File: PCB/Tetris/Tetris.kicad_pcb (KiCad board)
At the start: 2 copper layers, 135 x 56 mm, 51 parts, among them J1 Power, J2 PWM, J3 Analog, J4 PWM, J5 Analog, J6 Communication, J7 Digital, M1 RGBMatrix, M2 RGBMatrix, SW1 SW_Push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

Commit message: MASSIVE PROGRESS
Redesign PCB to use ports
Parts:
- removed U2: 74HC595, Package_DIP:DIP-16_W7.62mm_Socket_LongPads
- added J8: Digital, Connector_PinHeader_2.54mm:PinHeader_2x08_P2.54mm_Vertical, B.Cu at (188.4, 125.4)
- G2: renamed from Mr. G
- J1: footprint Connector_PinHeader_2.54mm:PinHeader_1x08_P2.54mm_Vertical -> Connector_PinHeader_2.54mm:PinHeader_1x02_P2.54mm_Vertical
- J2: footprint Connector_PinHeader_2.54mm:PinHeader_1x10_P2.54mm_Vertical -> Connector_PinHeader_2.54mm:PinHeader_1x07_P2.54mm_Vertical
- J4: footprint Connector_PinHeader_2.54mm:PinHeader_1x08_P2.54mm_Vertical -> Connector_PinHeader_2.54mm:PinHeader_1x06_P2.54mm_Vertical
- J7: footprint Connector_PinHeader_2.54mm:PinHeader_2x18_P2.54mm_Vertical -> Connector_PinHeader_2.54mm:PinHeader_2x09_P2.54mm_Vertical
- R1, R10, R11, R12, R2, R24, R25, R26, R27, R3, R4, R5, R6, R7, R8, R9: footprint Resistor_THT:R_Axial_DIN0207_L6.3mm_D2.5mm_P10.16mm_Horizontal -> RGBMatrix:R_Axial_DIN0207_L6.3mm_D2.5mm_P12.40mm_Horizontal
- R17, R18: footprint Resistor_THT:R_Axial_DIN0207_L6.3mm_D2.5mm_P10.16mm_Horizontal -> Resistor_THT:R_Axial_DIN0207_L6.3mm_D2.5mm_P7.62mm_Horizontal
- moved BZ1 74.1 mm to (159.2, 72.5), turned to 180 degrees
- moved R24 70.1 mm to (161.9, 77.0), turned to 180 degrees
- moved BZ2 63.3 mm to (144.3, 72.5), turned to 180 degrees
- moved BZ4 57.6 mm to (111.8, 72.7), turned to 180 degrees
- moved R25 57.3 mm to (146.7, 77.0), turned to 180 degrees
- moved BZ3 57.2 mm to (129.1, 72.7), turned to 180 degrees
- moved R26 50.1 mm to (131.7, 77.0), turned to 180 degrees
- moved R27 49.6 mm to (114.3, 76.8), turned to 180 degrees
- moved R23 27.1 mm to (206.1, 112.7), turned to -90 degrees
- moved SW5 26.9 mm to (202.9, 87.8), turned to -90 degrees
- moved R20 26.7 mm to (216.9, 126.7), turned to 90 degrees
- moved R19 25.6 mm to (216.9, 113.7), turned to 90 degrees
- moved SW6 24.9 mm to (202.9, 98.8), turned to -90 degrees
- moved R17 23.2 mm to (216.8, 89.6), turned to 90 degrees
- moved J7 22.9 mm to (188.4, 102.5)
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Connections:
- BZ1 pad 1: /*13 -> /*6
- BZ2 pad 1: /*12 -> /*7
- BZ3 pad 1: /*11 -> /*8
- BZ4 pad 1: /*10 -> /*9
- J1 pad 1: unconnected-(J1-Pin_1-Pad1) -> +5V
- J1 pad 2: /IOREF -> GND
- J2 pad 1: /SCL/21 -> GND
- J2 pad 2: /SDA/20 -> /*13
- J2 pad 3: /AREF -> /*12
- J2 pad 4: GND -> /*11
- J2 pad 5: /*13 -> /*10
- J2 pad 6: /*12 -> /*9
- J2 pad 7: /*11 -> /*8
- J6 pad 1: /TX3/14 -> /14
- J6 pad 2: /RX3/15 -> /15
- J6 pad 3: /TX2/16 -> /16
- J6 pad 4: /RX2/17 -> /17
- J6 pad 5: /TX1/18 -> /18
- J6 pad 6: /RX1/19 -> /19
- J6 pad 7: /SDA/20 -> /20
- J6 pad 8: /SCL/21 -> /21
- J7 pad 1: GND -> /36
- J7 pad 10: /47 -> /29
- J7 pad 11: /*44 -> /26
- J7 pad 12: /*45 -> /27
- J7 pad 13: /42 -> /24
- J7 pad 14: /43 -> /25
- J7 pad 15: /40 -> /22
- J7 pad 16: /41 -> /23
- J7 pad 17: /38 -> +5V
- J7 pad 18: /39 -> +5V
- J7 pad 2: GND -> /37
- J7 pad 3: /*52 -> /34
- J7 pad 4: /53 -> /35
- J7 pad 5: /50 -> /32
- J7 pad 6: /51 -> /33
- J7 pad 7: /48 -> /30
- J7 pad 8: /49 -> /31
- J7 pad 9: /*46 -> /28
- M1 pad 16: /*52 -> /A15
- M1 pad 21: /SCL/21 -> /22
- M1 pad 22: /SDA/20 -> /23
- M1 pad 23: /RX1/19 -> /24
- M1 pad 24: /TX1/18 -> /25
- M1 pad 25: /RX2/17 -> /26
- M1 pad 26: /TX2/16 -> /27
- M1 pad 27: /RX3/15 -> /28
- M1 pad 28: /TX3/14 -> /29
- M2 pad 1: /S1 -> /*13
- M2 pad 10: /S10 -> /43
- M2 pad 11: /S11 -> /*44
- M2 pad 12: /S12 -> /*45
- M2 pad 13: /S13 -> /*46
- M2 pad 14: /S14 -> /47
- M2 pad 15: /S15 -> /48
- M2 pad 16: /S16 -> /49
- M2 pad 2: /S2 -> /*12
- M2 pad 21: /*9 -> /37
- M2 pad 22: /*8 -> /36
- M2 pad 23: /*7 -> /35
- M2 pad 24: /*6 -> /34
- M2 pad 25: /*5 -> /33
- M2 pad 26: /*4 -> /32
- M2 pad 27: /*3 -> /31
- M2 pad 28: /*2 -> /30
- M2 pad 3: /S3 -> /*11
- M2 pad 4: /S4 -> /*10
- M2 pad 5: /S5 -> /50
- M2 pad 6: /S6 -> /51
- M2 pad 7: /S7 -> /*52
- M2 pad 8: /S8 -> /53
- M2 pad 9: /S9 -> /42
- R1 pad 1: /30 -> /S1
- R10 pad 1: /28 -> /S2
- R11 pad 1: /26 -> /S3
- R12 pad 1: /24 -> /S4
- R13 pad 2: /32 -> /S5
- R14 pad 2: /34 -> /S6
- R15 pad 2: /36 -> /S7
- R16 pad 2: /38 -> /S8
- R17 pad 2: /23 -> /19
- R18 pad 2: /27 -> /20
- R19 pad 2: /31 -> /18
- R2 pad 1: /28 -> /S2
- R20 pad 2: /41 -> /15
- R21 pad 2: /33 -> /16
- R22 pad 1: /37 -> /17
- R23 pad 1: /25 -> /21
- R3 pad 1: /26 -> /S3
- R4 pad 1: /24 -> /S4
- R5 pad 2: /32 -> /S5
- R6 pad 2: /34 -> /S6
- R7 pad 2: /36 -> /S7
- R8 pad 2: /38 -> /S8
- R9 pad 1: /30 -> /S1
- SW1 pad 1: /23 -> /19
- SW2 pad 1: /27 -> /20
- SW3 pad 1: /31 -> /18
- SW4 pad 1: /41 -> /15
- SW5 pad 1: /33 -> /16
- SW6 pad 1: /37 -> /17
- SW7 pad 1: /25 -> /21
- U1 pad 11: /42 -> /*4
- U1 pad 12: /40 -> /*5
- U1 pad 14: /*44 -> /40
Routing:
- net /43: track 0.00 -> 115.1 mm, vias 0 -> 3
- net /51: track 0.00 -> 109.1 mm, vias 0 -> 2
- net /15: track 0.00 -> 102.6 mm
- net /38: track 98.3 -> 0.00 mm
- net /53: track 0.00 -> 96.7 mm, vias 0 -> 2
- net /*45: track 0.00 -> 95.8 mm
- net GND: track 181.0 -> 272.7 mm, vias 0 -> 2
- net /35: track 0.00 -> 86.2 mm
- net /47: track 0.00 -> 84.6 mm
- net /18: track 0.00 -> 82.0 mm
- net /*52: track 4.34 -> 78.8 mm
- net /29: track 0.00 -> 72.5 mm
- net /49: track 0.00 -> 72.2 mm
- net /31: track 33.2 -> 104.1 mm
- net /17: track 0.00 -> 67.8 mm
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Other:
- board size 135 x 56 mm -> 133.5 x 65.3 mm
- board text added: "Jonathan Cai 2023 Thanks: Evan Tao"
- board text added: "Mr. G"
- board text removed: "Jonathan Cai 2023"

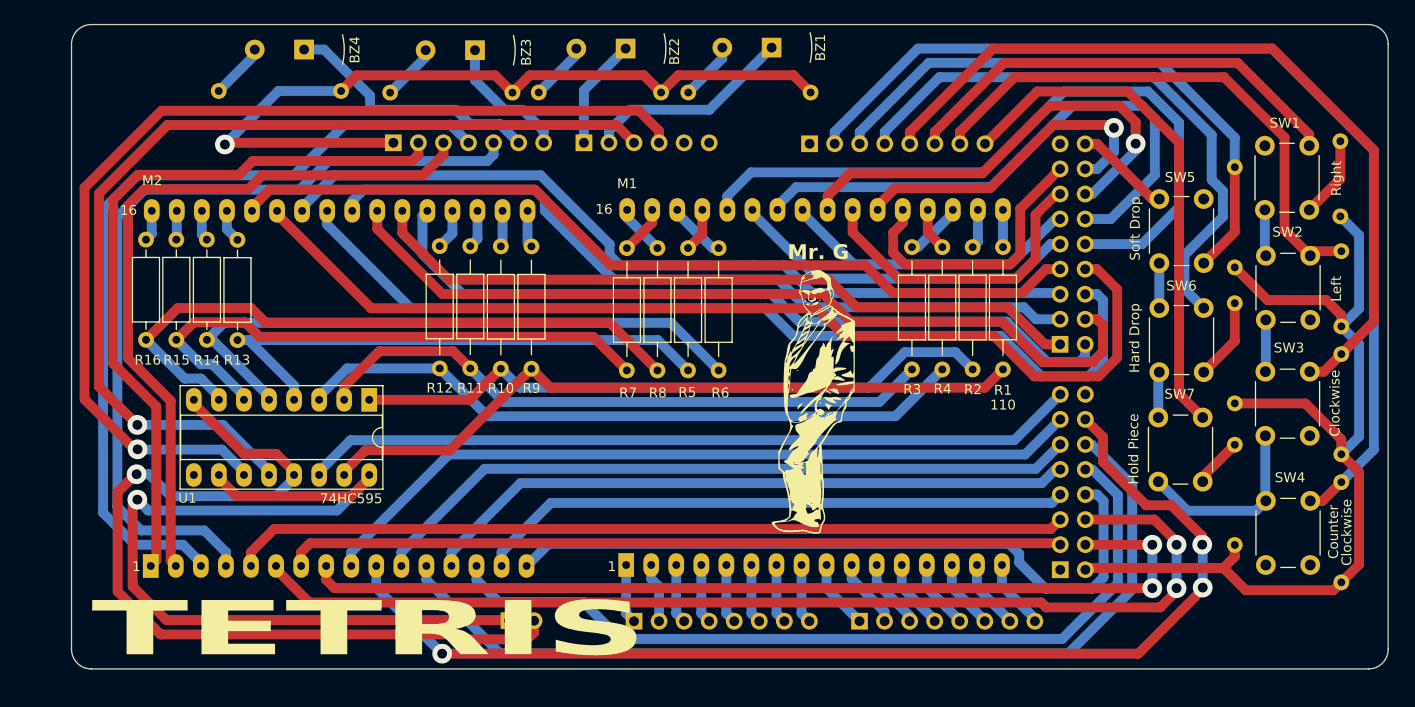
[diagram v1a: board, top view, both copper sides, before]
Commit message: Cleaned up and tidy repository
Removed duplicated/unwanted PCB files,

Added pictures for read me
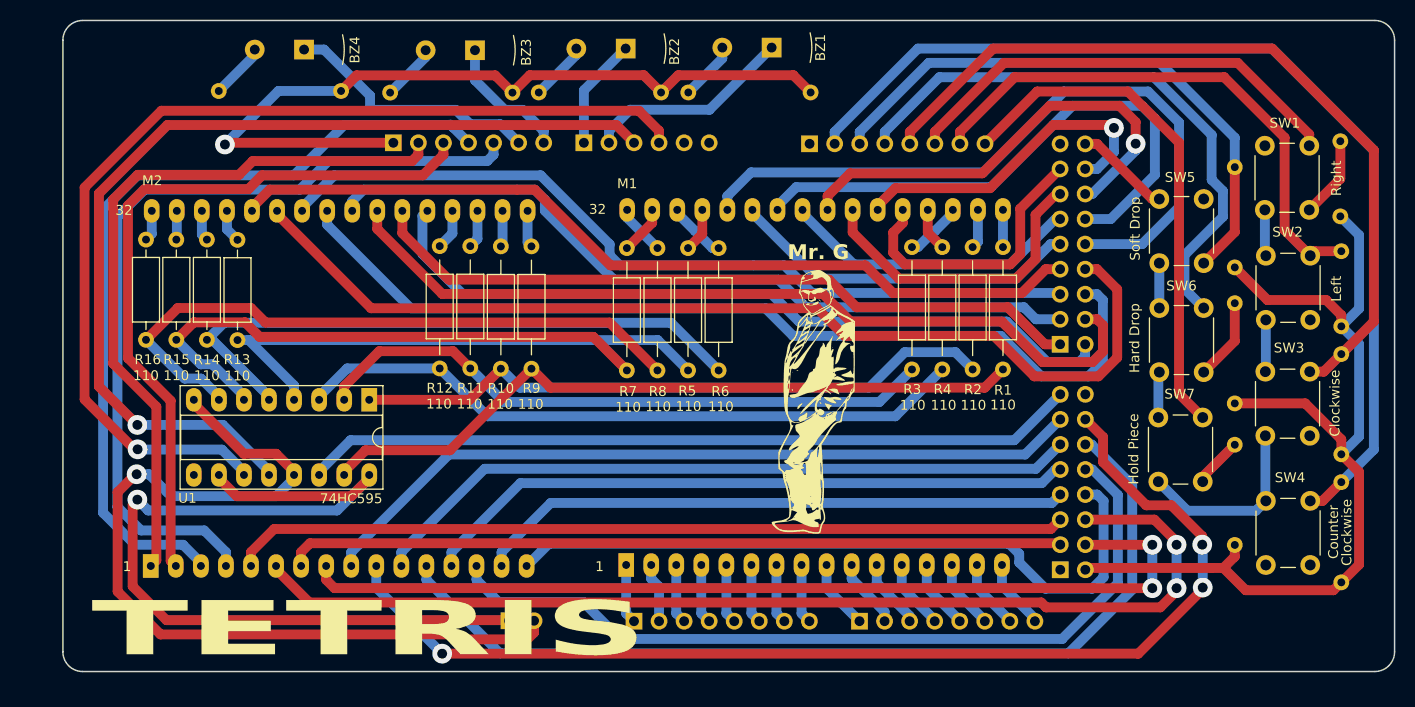
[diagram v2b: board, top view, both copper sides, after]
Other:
- board size 133.5 x 65.3 mm -> 135 x 66 mm
- board text added: "Jonathan Cai 2023"
- board text added: "Thanks: Evan Tao"
- board text removed: "Jonathan Cai 2023 Thanks: Evan Tao"
